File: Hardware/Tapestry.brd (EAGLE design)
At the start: 95.2 x 67.3 mm, 94 parts, among them J1 CORTEX_DEBUGPTH, U1 ATSAMS70NXXA-AN, U2 AK4618VQSFE-PACKAGE, Y1 12MHz

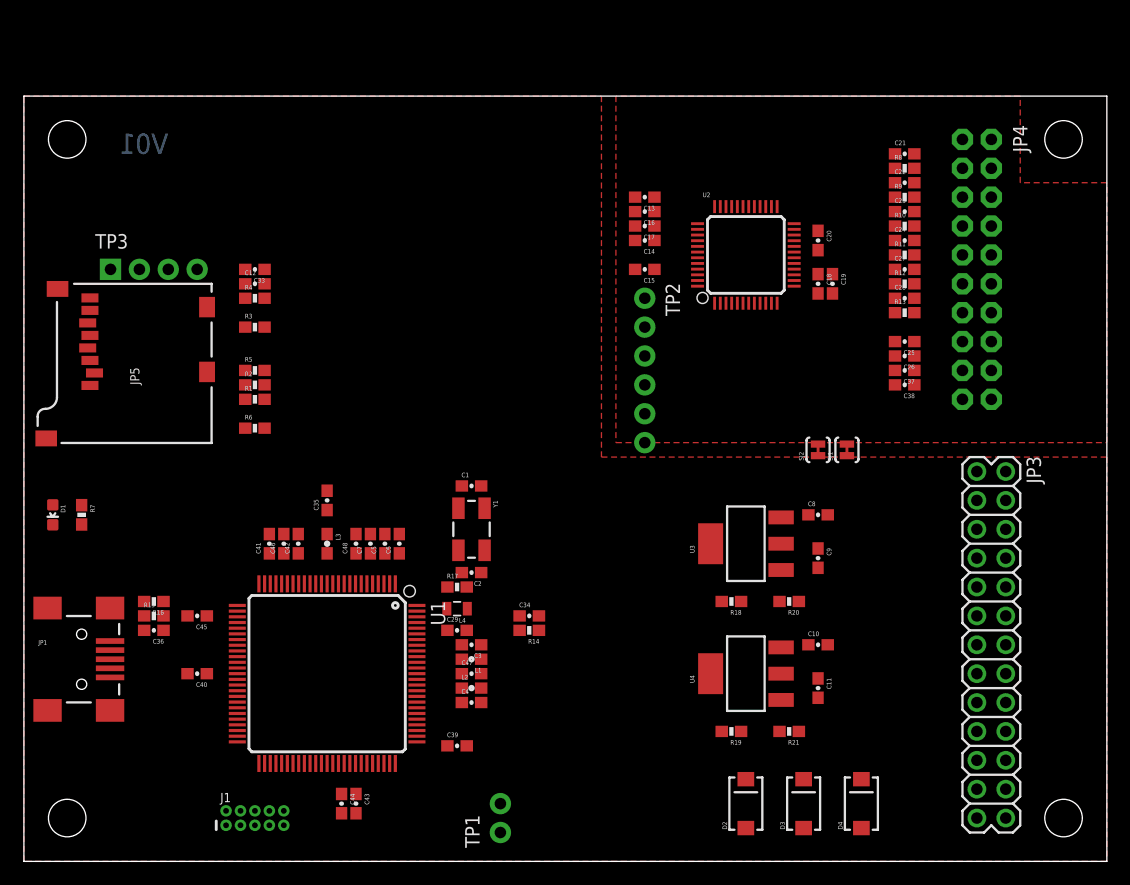
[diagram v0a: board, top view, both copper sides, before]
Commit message: More updates.
Schematic logos, partitioning & labeling.
Found a few more absent pullup resistors.
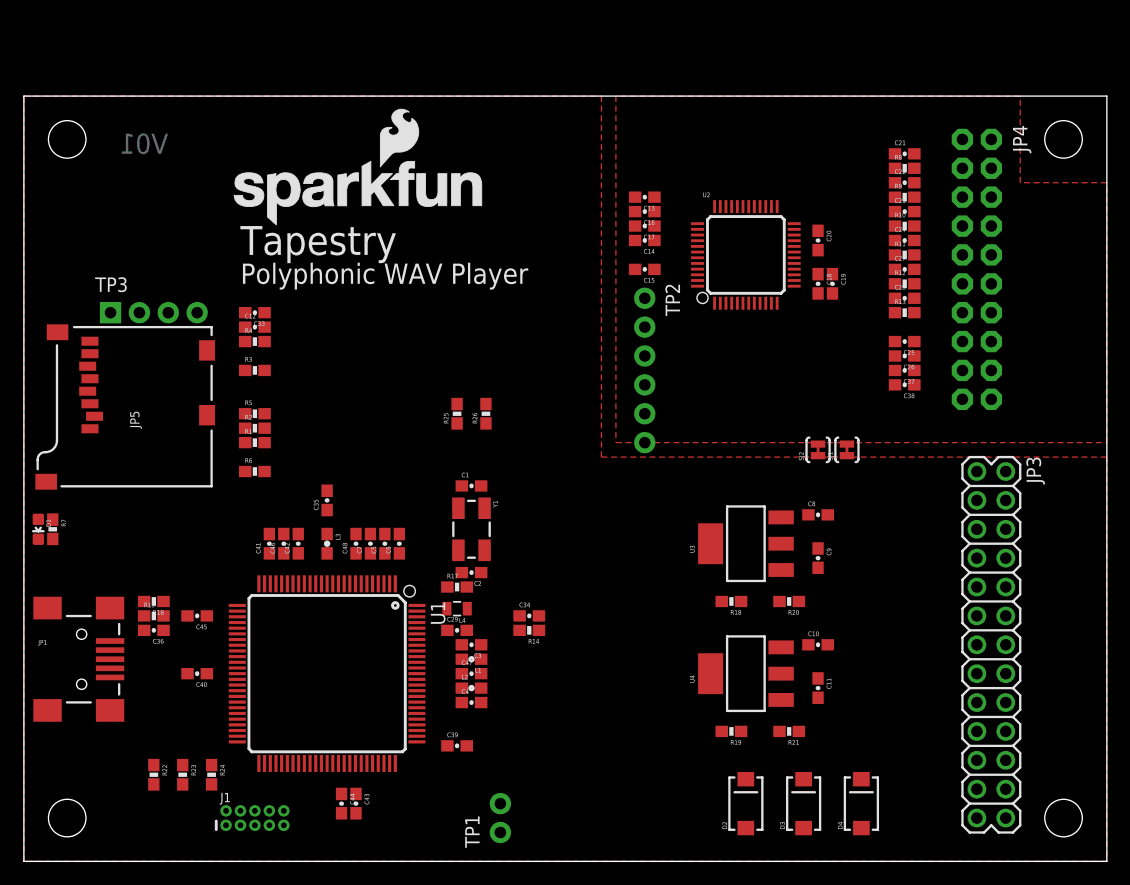
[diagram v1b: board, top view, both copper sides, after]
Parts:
- added LOGO1: SFE_LOGO_NAME_FLAME.2_INCH, SparkFun-Aesthetics:SFE_LOGO_NAME_FLAME_.2
- added R22, R23, R24: 100k, SparkFun-Resistors:0603-RES
- added R25, R26: 4.7K, SparkFun-Resistors:0603-RES
- moved C33 3.81 mm to (20.3, 48.3)
- moved R1 3.81 mm to (20.3, 36.8)
- moved R3 3.81 mm to (20.3, 43.2)
- moved R4 3.81 mm to (20.3, 45.7)
- moved R5 3.81 mm to (20.3, 39.4)
- moved R6 3.81 mm to (20.3, 34.3)
- moved TP3 3.81 mm to (7.62, 48.3)
- moved C12 3.81 mm to (20.3, 47.0)
- moved JP5 3.81 mm to (16.5, 33.0)
- moved R2 3.81 mm to (20.3, 38.1)
- moved R7 2.84 mm to (2.54, 29.2)
- moved D1 1.80 mm to (1.27, 29.2)
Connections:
- net 3.3V: now also R22.2, R23.2, R24.2, R25.2, R26.2
- net I2C_SCK: now also R26.1
- net I2C_SDA: now also R25.1
- net NRESET: now also R24.1
- net SWCLK/TCK: now also R23.1
- net SWDIO/TMS: now also R22.1
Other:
- board text added: "Polyphonic WAV Player"
- board text added: "Tapestry"

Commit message: WIP.
Checking in so I can traverse project history for a moment.
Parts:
- added J2: POWER_JACKPTH_LOCK, SparkFun-Connectors:POWER_JACK_PTH_LOCK
- moved D3 31.1 mm to (74.9, 35.6), turned to 0 degrees
- moved D2 30.6 mm to (66.0, 35.6), turned to 0 degrees
- moved JP3 29.2 mm to (72.2, 7.45), turned to 180 degrees
- moved D4 26.7 mm to (74.9, 31.8), turned to 180 degrees
- moved C11 23.6 mm to (55.9, 34.2)
- moved R19 23.6 mm to (48.2, 30.4)
- moved R21 23.6 mm to (53.3, 30.4)
- moved U4 23.6 mm to (49.5, 35.5)
- moved C10 23.6 mm to (55.9, 38.0)
- moved TP1 8.00 mm to (33.9, 2.54)
- moved TP2 6.48 mm to (53.3, 55.9)
- moved C14 4.58 mm to (57.1, 58.4)
- moved C15 4.58 mm to (57.1, 55.9)
- moved C16 4.58 mm to (57.1, 61.0)
- moved C13 4.58 mm to (57.1, 62.2)
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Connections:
- net GND: now also J2.GND, J2.GNDBREAK
- net VIN: now also J2.PWR

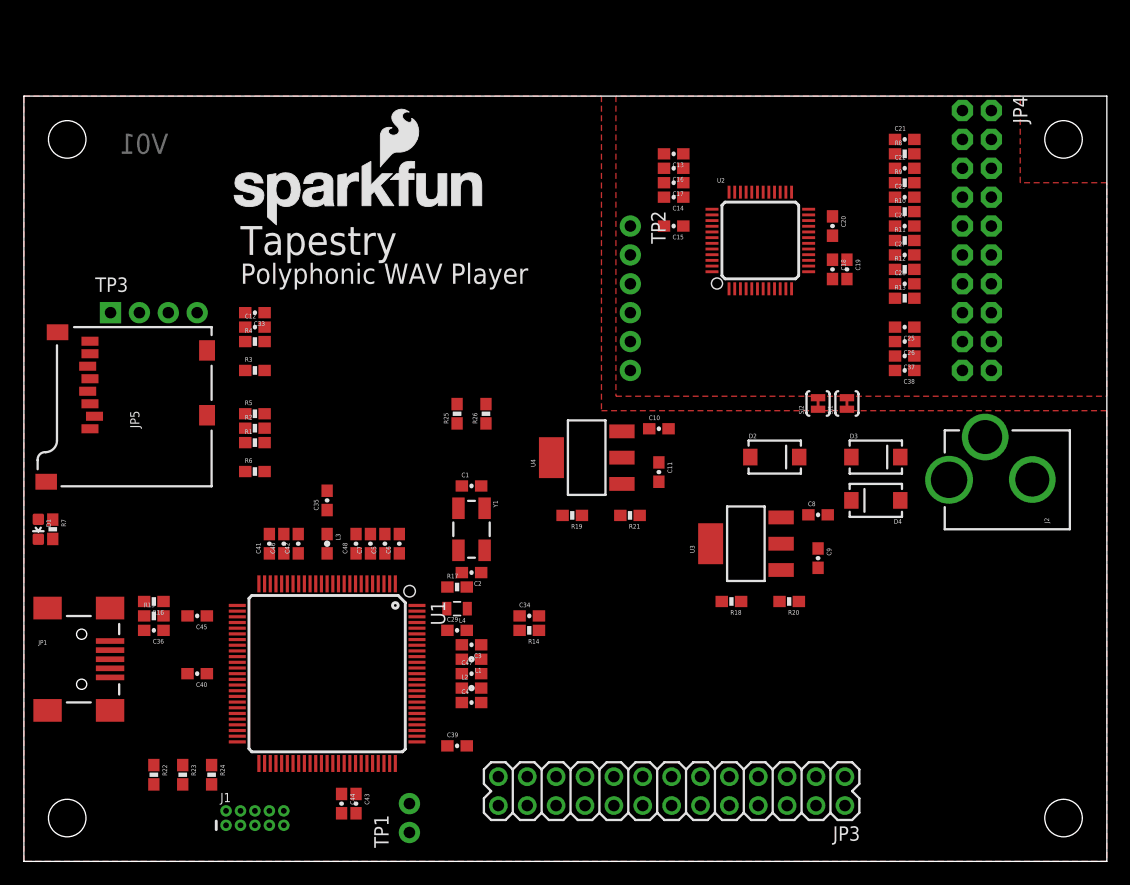
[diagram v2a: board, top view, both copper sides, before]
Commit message: Added reset switch & some labeling.
Still WIP.
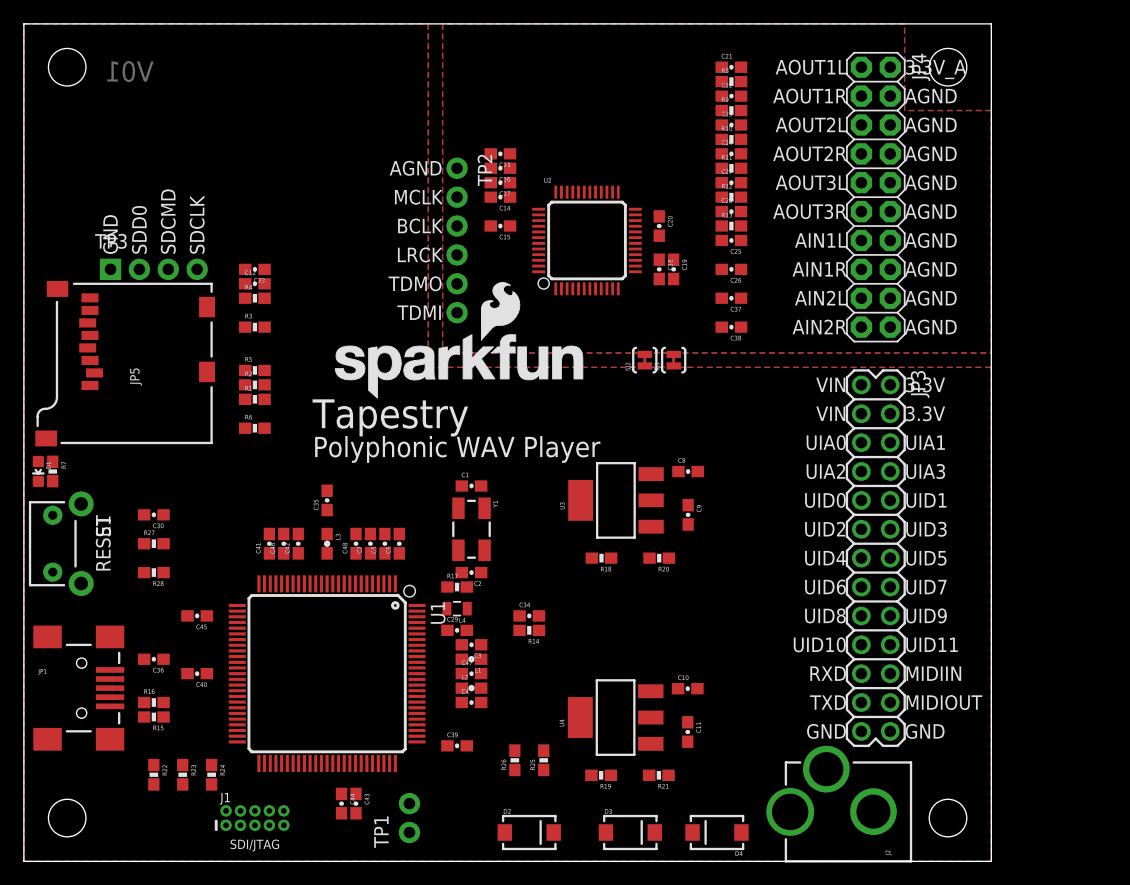
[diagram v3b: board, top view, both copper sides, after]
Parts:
- added C30: 10nF, SparkFun-Capacitors:0603-CAP
- added R27: 33, SparkFun-Resistors:0603-RES
- added R28: 10K, SparkFun-Resistors:0603-RES
- added S1: RESET SW, SparkFun-Electromechanical:TACTILE-PTH-SIDEEZ
- JP4: device SparkFun-Connectors:2X10_NOSILK -> SparkFun-Connectors:2X10
- moved D2 39.5 mm to (44.5, 2.54)
- moved D3 39.5 mm to (53.3, 2.54)
- moved JP3 34.5 mm to (73.7, 41.9), turned to 270 degrees
- moved D4 32.4 mm to (61.0, 2.54)
- moved J2 32.4 mm to (81.3, 4.35)
- moved R25 31.4 mm to (45.7, 8.89)
- moved R26 30.6 mm to (43.2, 8.89)
- moved C10 23.0 mm to (58.4, 15.2)
- moved C11 23.0 mm to (58.4, 11.4)
- moved R19 23.0 mm to (50.8, 7.57)
- moved R21 23.0 mm to (55.9, 7.57)
- moved U4 23.0 mm to (52.0, 12.7)
- moved LOGO1 17.6 mm to (26.7, 40.6)
- moved C25 17.0 mm to (62.2, 54.6)
- moved R9 16.5 mm to (62.2, 66.0)
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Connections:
- new net N$26: R27.1, S1.2
- net 3.3V: now also R28.2
- net GND: now also C30.2, S1.1
- net NRESET: now also C30.1, R27.2, R28.1
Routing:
- added copper zone on layer 16, net GND
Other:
- board size 95.2 x 67.3 mm -> 85.1 x 73.7 mm
- board text added: "3.3V"
- board text added: "3.3V_A"
- board text added: "AGND"
- board text added: "AIN1L"
- board text added: "AIN1R"
- board text added: "AIN2L"
- board text added: "AIN2R"
- board text added: "AOUT1L"
- board text added: "AOUT1R"
- board text added: "AOUT2L"
- board text added: "AOUT2R"
- board text added: "AOUT3L"
- board text added: "AOUT3R"
- board text added: "BCLK"
- board text added: "GND"
- board text added: "LRCK"
- board text added: "MCLK"
- board text added: "MIDIIN"
- board text added: "MIDIOUT"
- board text added: "RESET"
- board text added: "RXD"
- board text added: "SDCLK"
- board text added: "SDCMD"
- board text added: "SDD0"
- board text added: "SDI/JTAG"
- board text added: "TDMI"
- board text added: "TDMO"
- board text added: "TXD"
- board text added: "UIA0"
- board text added: "UIA1"
- board text added: "UIA2"
- board text added: "UIA3"
- board text added: "UID0"
- board text added: "UID1"
- board text added: "UID10"
- board text added: "UID11"
- board text added: "UID2"
- board text added: "UID3"
- board text added: "UID4"
- board text added: "UID5"
- board text added: "UID6"
- board text added: "UID7"
- board text added: "UID8"
- board text added: "UID9"
- board text added: "VIN"

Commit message: Continuing work.
Labeling, & sizing mostly complete.

About ready to route.
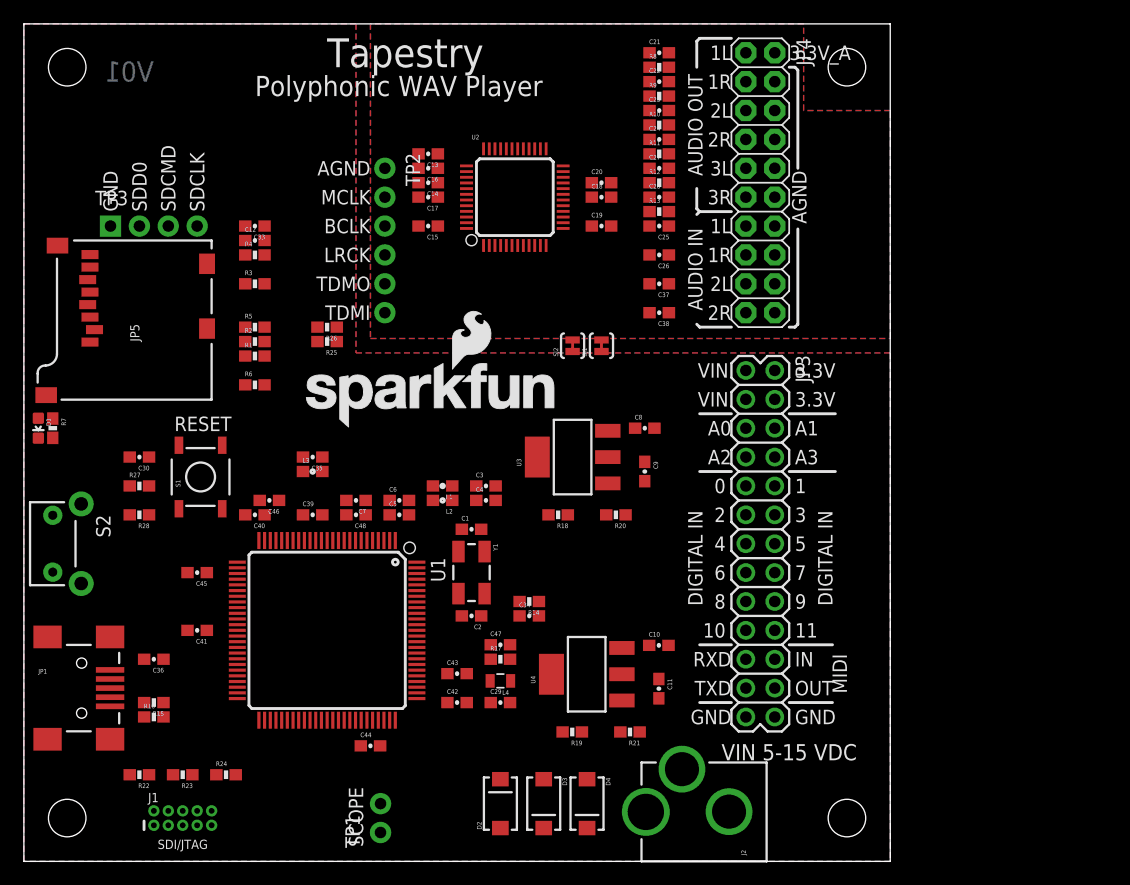
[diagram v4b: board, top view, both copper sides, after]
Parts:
- added S2: DNS, SparkFun-Electromechanical:TACTILE-PTH-SIDEEZ
- JP3: value (none) -> I/O
- JP4: value (none) -> AUDIO I/O
- S1: value RESET SW -> RESET; device SparkFun-Electromechanical:TACTILE-PTH-SIDEEZ -> SparkFun-Electromechanical:TACTILE-SWITCH-SMD
- TP1: value (none) -> Trigger
- TP2: value (none) -> I2S TP
- TP3: value (none) -> SD TP
- U3, U4: value (none) -> LM1117
- moved FRAME1 105.1 mm to (-1.27, -20.3)
- moved R26 41.5 mm to (26.7, 47.0), turned to 180 degrees
- moved R25 41.5 mm to (26.7, 45.7), turned to 180 degrees
- moved C39 24.0 mm to (25.4, 30.5)
- moved C42 19.8 mm to (38.1, 14.0), turned to 0 degrees
- moved C4 17.8 mm to (40.6, 31.8)
- moved L2 16.7 mm to (36.8, 31.8), turned to 180 degrees
- moved L1 15.5 mm to (36.8, 33.0)
- moved C40 14.9 mm to (20.3, 30.5)
- moved C43 14.5 mm to (38.1, 16.5), turned to 0 degrees
- moved S1 14.3 mm to (15.5, 33.8), turned to 90 degrees
- moved C3 14.0 mm to (40.6, 33.0), turned to 0 degrees
- moved J2 12.7 mm to (68.6, 4.35)
- moved D4 11.7 mm to (49.5, 5.08), turned to 270 degrees
- moved JP4 10.2 mm to (64.8, 59.7)
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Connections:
- net GND: now also S2.1
- net N$26: now also S1.3, S2.2; no longer S1.2
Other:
- board size 85.1 x 73.7 mm -> 76.2 x 73.7 mm
- board text added: "0"
- board text added: "1"
- board text added: "10"
- board text added: "11"
- board text added: "1L"
- board text added: "1R"
- board text added: "2"
- board text added: "2L"
- board text added: "2R"
- board text added: "3"
- board text added: "3L"
- board text added: "3R"
- board text added: "4"
- board text added: "5"
- board text added: "6"
- board text added: "7"
- board text added: "8"
- board text added: "9"
- board text added: "A0"
- board text added: "A1"
- board text added: "A2"
- board text added: "A3"
- board text added: "AUDIO IN"
- board text added: "AUDIO OUT"
- board text added: "DIGITAL IN"
- board text added: "IN"
- board text added: "MIDI"
- board text added: "OUT"
- board text added: "SCOPE"
- board text added: "VIN 5-15 VDC"
- board text removed: "AIN1L"
- board text removed: "AIN1R"
- board text removed: "AIN2L"
- board text removed: "AIN2R"
- board text removed: "AOUT1L"
- board text removed: "AOUT1R"
- board text removed: "AOUT2L"
- board text removed: "AOUT2R"
- board text removed: "AOUT3L"
- board text removed: "AOUT3R"
- board text removed: "MIDIIN"
- board text removed: "MIDIOUT"
- board text removed: "UIA0"
- board text removed: "UIA1"
- board text removed: "UIA2"
- board text removed: "UIA3"
- board text removed: "UID0"
- board text removed: "UID1"
- board text removed: "UID10"
- board text removed: "UID11"
- board text removed: "UID2"
- board text removed: "UID3"
- board text removed: "UID4"
- board text removed: "UID5"
- board text removed: "UID6"
- board text removed: "UID7"
- board text removed: "UID8"
- board text removed: "UID9"

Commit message: Ready to start routing.
If I need to fall back, this is the one.
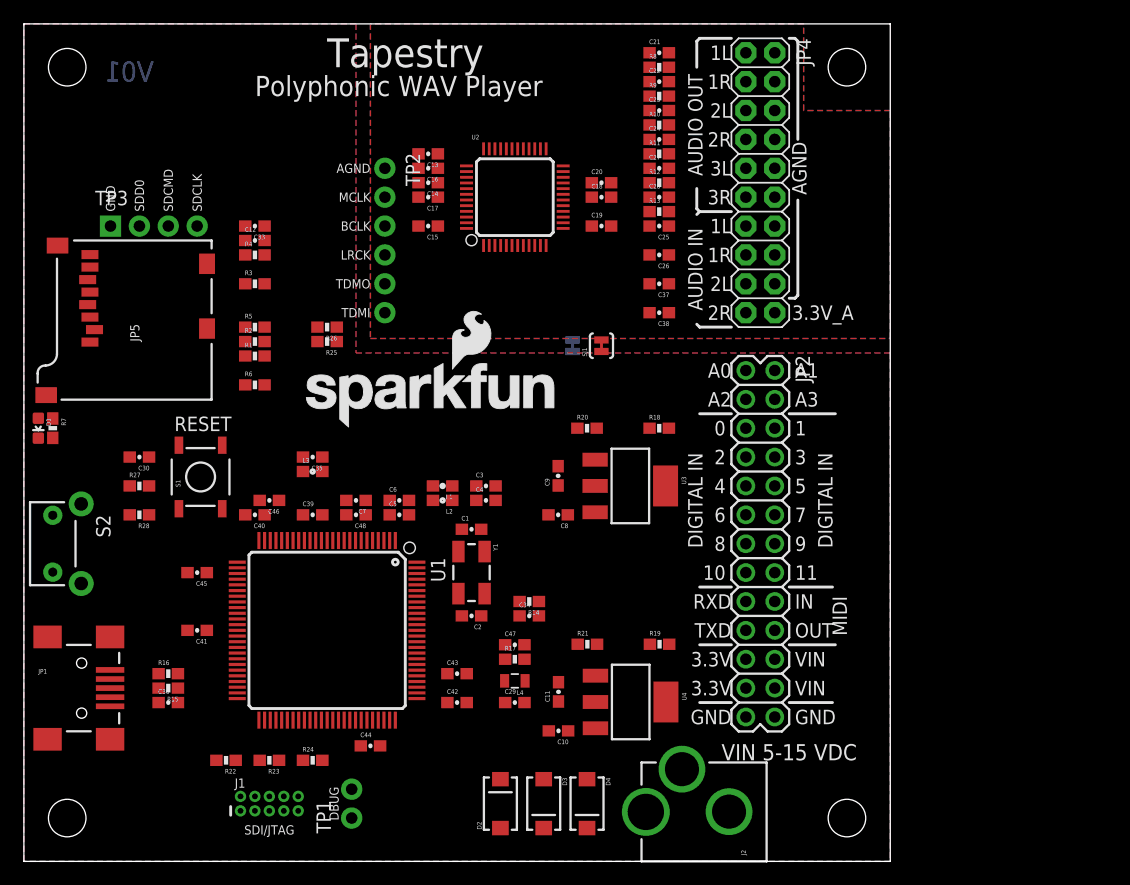
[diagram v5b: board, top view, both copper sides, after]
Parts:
- moved R18 11.7 mm to (55.9, 38.1), turned to 0 degrees
- moved C10 11.6 mm to (47.0, 11.5), turned to 180 degrees
- moved R19 10.9 mm to (55.9, 19.1), turned to 0 degrees
- moved C8 10.8 mm to (47.0, 30.5), turned to 180 degrees
- moved C11 8.83 mm to (47.0, 14.9), turned to 90 degrees
- moved R21 8.58 mm to (49.6, 19.1), turned to 0 degrees
- moved R20 8.03 mm to (49.5, 38.1), turned to 0 degrees
- moved R22 7.73 mm to (17.8, 8.89)
- moved R23 7.73 mm to (21.6, 8.89)
- moved J1 7.73 mm to (21.6, 5.08)
- moved R24 7.73 mm to (25.4, 8.89)
- moved C9 7.63 mm to (47.0, 33.9), turned to 90 degrees
- moved U3 5.68 mm to (53.3, 33.0), turned to 270 degrees
- moved U4 4.57 mm to (53.4, 14.0), turned to 270 degrees
- moved R16 4.02 mm to (12.7, 16.5)
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- renumbered JP3 to JP2
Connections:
- net 3.3V: now also JP2.21, JP2.23; no longer JP2.2, JP2.4
- net 3.3V_A: now also JP4.20; no longer JP4.2
- net GND: now also JP4.2; no longer JP4.20
- net MIN: now also JP2.18; no longer JP2.22
- net MOUT: now also JP2.20; no longer JP2.24
- net RXD: now also JP2.17; no longer JP2.21
- net TXD: now also JP2.19; no longer JP2.23
- net UIA0: now also JP2.1; no longer JP2.5
- net UIA1: now also JP2.2; no longer JP2.6
- net UIA2: now also JP2.3; no longer JP2.7
- net UIA3: now also JP2.4; no longer JP2.8
- net UID0: now also JP2.5; no longer JP2.9
- net UID1: now also JP2.6; no longer JP2.10
- net UID10: now also JP2.15; no longer JP2.19
- net UID11: now also JP2.16; no longer JP2.20
- net UID2: now also JP2.7; no longer JP2.11
- net UID3: now also JP2.8; no longer JP2.12
- net UID4: now also JP2.9; no longer JP2.13
- net UID5: now also JP2.10; no longer JP2.14
- net UID6: now also JP2.11; no longer JP2.15
- net UID7: now also JP2.12; no longer JP2.16
- net UID8: now also JP2.13; no longer JP2.17
- net UID9: now also JP2.14; no longer JP2.18
- net VIN: now also JP2.22, JP2.24; no longer JP2.1, JP2.3
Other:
- board text added: "DBUG"
- board text removed: "SCOPE"
